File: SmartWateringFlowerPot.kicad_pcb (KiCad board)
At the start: 2 copper layers, 61.9 x 80.9 mm, 36 parts, among them J1 USB-C 5V + USB2, J2 PUMP 5V, J3 MOISTURE, J4 RESERVOIR_SW, J5 FLOW optional, J6 UI OLED/ENC/LED, J7 DEBUG 3V3/GND/TX/RX/EN/BOOT, Q1 AO3400A, U1 ESP32-S3-WROOM-1-N8, U2 AP63203WU-7

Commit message: Prepare clean order batch package
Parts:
- C4, R8: moved to B.Cu
- moved C4 36.9 mm to (106.0, 72.5), turned to 90 degrees
- moved R8 25.8 mm to (92.6, 115.2), turned to 180 degrees
- moved R6 20.7 mm to (64.0, 93.0)
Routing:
- net Net-(J7-Pin_5): track 168.6 -> 115.6 mm, vias 0 -> 1
- net +3V3: track 802.2 -> 824.0 mm, vias 0 -> 2
- net Net-(J6-Pin_5): track 0.00 -> 11.7 mm
- net Net-(J4-Pin_1): track 33.6 -> 44.3 mm, vias 2 -> 3
- net Net-(J6-Pin_3): track 14.8 -> 22.7 mm
- net GND: track 455.7 -> 448.3 mm
- net Net-(TP5-Pin_1): track 128.6 -> 129.6 mm

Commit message: Rebrand order package and add five-unit BOM
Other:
- board text added: "Self-Watering Flower Pot V2 Rev A By Christopher Heskett For the TETC"
- board text removed: "{dblquote}Self Watering Flower Pot{dblquote} By Christopher Heskett For the TETC"
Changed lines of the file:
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@@
 		(layer "Edge.Cuts")
 	)
-	(gr_text "{dblquote}Self Watering Flower Pot{dblquote}\nBy Christopher Heskett\nFor the TETC"
+	(gr_text "Self-Watering Flower Pot V2 Rev A\nBy Christopher Heskett\nFor the TETC"
 		(at 86.07 51.63 0)
 		(layer "F.SilkS")

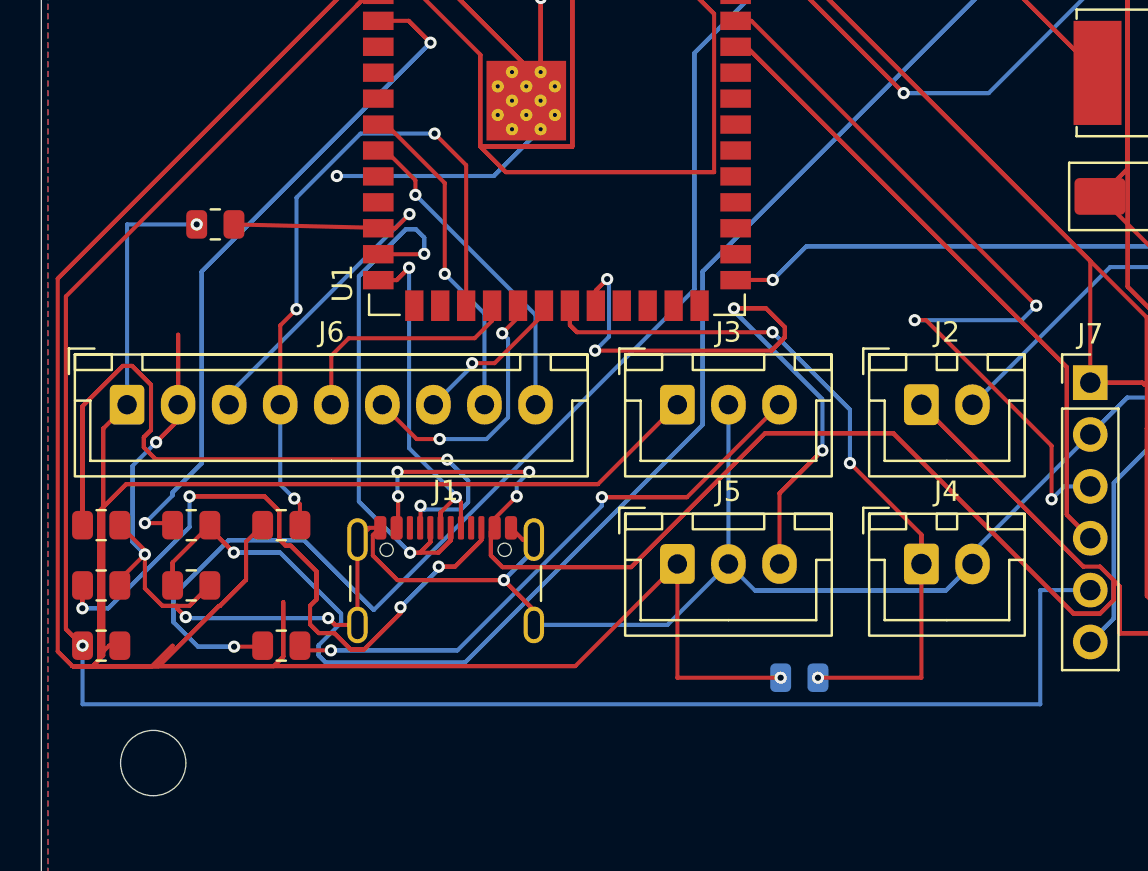
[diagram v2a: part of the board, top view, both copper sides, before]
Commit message: Implement board-a-only cost-down redesign
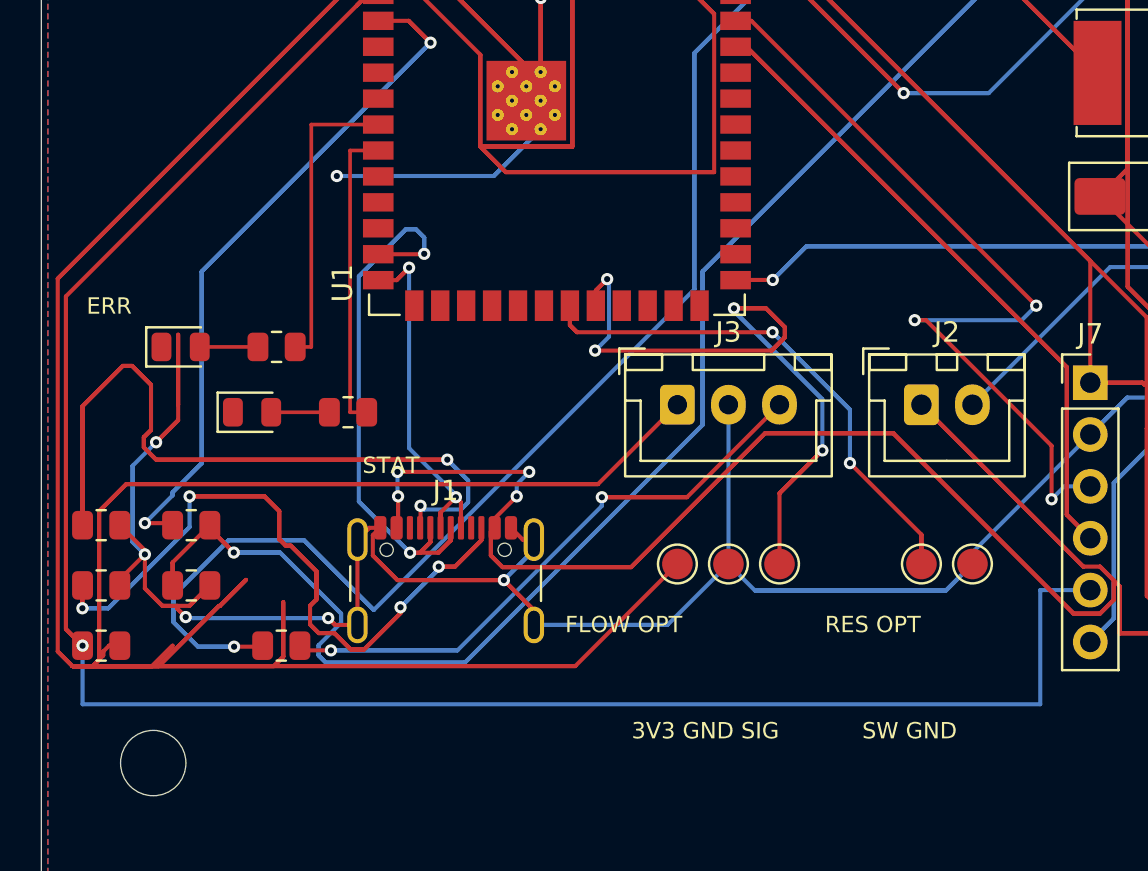
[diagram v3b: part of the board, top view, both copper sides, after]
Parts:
- removed J4: RESERVOIR_SW, Connector_JST:JST_XH_B2B-XH-A_1x02_P2.50mm_Vertical
- removed J5: FLOW optional, Connector_JST:JST_XH_B3B-XH-A_1x03_P2.50mm_Vertical
- removed J6: UI OLED/ENC/LED, Connector_JST:JST_XH_B9B-XH-A_1x09_P2.50mm_Vertical
- removed R6: 4.7k SDA, Resistor_SMD:R_0805_2012Metric
- removed R7: 4.7k SCL, Resistor_SMD:R_0805_2012Metric
- removed R8: 10k reservoir pullup, Resistor_SMD:R_0805_2012Metric
- added D2: ERROR red, LED_SMD:LED_0805_2012Metric, F.Cu at (62.3, 99.0)
- added D3: STATUS green, LED_SMD:LED_0805_2012Metric, F.Cu at (65.8, 102.2)
- added R11: 330R error LED, Resistor_SMD:R_0805_2012Metric, F.Cu at (67.0, 99.0)
- added R12: 330R status LED, Resistor_SMD:R_0805_2012Metric, F.Cu at (70.5, 102.2)
- added TP10: FLOW_PULSE optional pad, TestPoint:TestPoint_Pad_D1.5mm, F.Cu at (91.6, 109.6)
- added TP6: RESERVOIR_SW optional pad, TestPoint:TestPoint_Pad_D1.5mm, F.Cu at (98.6, 109.6)
- added TP7: OPT_GND pad, TestPoint:TestPoint_Pad_D1.5mm, F.Cu at (101.1, 109.6)
- added TP8: OPT_3V3 pad, TestPoint:TestPoint_Pad_D1.5mm, F.Cu at (86.6, 109.6)
- added TP9: OPT_GND pad, TestPoint:TestPoint_Pad_D1.5mm, F.Cu at (89.1, 109.6)
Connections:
- U1 pad 21: Net-(J4-Pin_1) -> /RESERVOIR_SW
- U1 pad 22: Net-(J5-Pin_3) -> /FLOW_PULSE
- U1 pad 8: Net-(J6-Pin_8) -> /ERROR_LED
- U1 pad 9: Net-(J6-Pin_9) -> /STATUS_LED
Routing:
- net +3V3: track 824.0 -> 772.7 mm, vias 2 -> 0
- net Net-(J5-Pin_3): track 47.9 -> 0.00 mm, vias 4 -> 0
- net /FLOW_PULSE: track 0.00 -> 47.9 mm, vias 0 -> 4
- net Net-(J4-Pin_1): track 44.3 -> 0.00 mm, vias 3 -> 0
- net Net-(U1-IO9): track 33.9 -> 0.00 mm, vias 3 -> 0
- net /RESERVOIR_SW: track 0.00 -> 33.6 mm, vias 0 -> 2
- net Net-(U1-IO8): track 22.7 -> 0.00 mm, vias 1 -> 0
- net Net-(J6-Pin_8): track 16.1 -> 0.00 mm, vias 1 -> 0
- net Net-(J6-Pin_9): track 15.8 -> 0.00 mm, vias 1 -> 0
- net /STATUS_LED: track 0.00 -> 15.0 mm
- net /ERROR_LED: track 0.00 -> 15.0 mm
- net Net-(U1-IO11): track 13.2 -> 0.00 mm, vias 2 -> 0
- net Net-(U1-IO10): track 11.7 -> 0.00 mm
- net Net-(U1-IO12): track 7.74 -> 0.00 mm, vias 1 -> 0
- net /STAT_LED_A: track 0.00 -> 2.85 mm
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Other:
- board text added: "3V3 GND SIG"
- board text added: "ERR"
- board text added: "FLOW OPT"
- board text added: "RES OPT"
- board text added: "STAT"
- board text added: "SW GND"

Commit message: Fix cost-down USB-C edge clearance
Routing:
- net Net-(J7-Pin_5): track 115.6 -> 113.2 mm
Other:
- outline, holes or cut-outs redrawn
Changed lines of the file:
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@@
 		(layer "Cmts.User")
 	)
-	(gr_rect
-		(start 55.48 44.18)
+	(gr_line
+		(start 82.5 116)
+		(end 68 116)
+		(stroke
+			(width 0.05)
+			(type default)
+		)
+		(layer "Edge.Cuts")
+	)
+	(gr_line
+		(start 68 125.12)
+		(end 55.48 125.12)
+		(stroke
+			(width 0.05)
+			(type default)
+		)
+		(layer "Edge.Cuts")
+	)
+	(gr_line
+		(start 117.37 44.18)
 		(end 117.37 125.12)
 		(stroke
@@
 			(type default)
 		)
-		(fill no)
+		(layer "Edge.Cuts")
+	)
+	(gr_line
+		(start 82.5 125.12)
+		(end 82.5 116)
+		(stroke
+			(width 0.05)
+			(type default)
+		)
+		(layer "Edge.Cuts")
+	)
+	(gr_line
+		(start 68 116)
+		(end 68 125.12)
+		(stroke
+			(width 0.05)
+			(type default)
+		)
+		(layer "Edge.Cuts")
+	)
+	(gr_line
+		(start 55.48 44.18)
+		(end 117.37 44.18)
+		(stroke
+			(width 0.05)
+			(type default)
+		)
+		(layer "Edge.Cuts")
+	)
+	(gr_line
+		(start 117.37 125.12)
+		(end 82.5 125.12)
+		(stroke
+			(width 0.05)
+			(type default)
+		)
+		(layer "Edge.Cuts")
+	)
+	(gr_line
+		(start 55.48 125.12)
+		(end 55.48 44.18)
+		(stroke
+			(width 0.05)
+			(type default)
+		)
 		(layer "Edge.Cuts")
 	)
@@
 	)
 	(segment
-		(start 106.85 110.91)
-		(end 104.4 110.91)
-		(width 0.2)
+		(start 104.4 115.3)
+		(end 57.498 115.3)
+		(width 0.18)
 		(layer "B.Cu")
 		(net 13)
 	)
 	(segment
-		(start 104.4 116.5)
-		(end 57.498 116.5)
-		(width 0.2)
+		(start 104.4 110.91)
+		(end 104.4 115.3)
+		(width 0.18)
 		(layer "B.Cu")
 		(net 13)
 	)
 	(segment
-		(start 57.498 116.5)
+		(start 57.498 115.3)
 		(end 57.498 113.63)
-		(width 0.2)
+		(width 0.18)
 		(layer "B.Cu")
 		(net 13)
 	)
 	(segment
-		(start 104.4 110.91)
-		(end 104.4 116.5)
-		(width 0.2)
+		(start 106.85 110.91)
+		(end 104.4 110.91)
+		(width 0.18)
 		(layer "B.Cu")
 		(net 13)
